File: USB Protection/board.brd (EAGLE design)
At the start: 22.9 x 15.2 mm, 6 parts

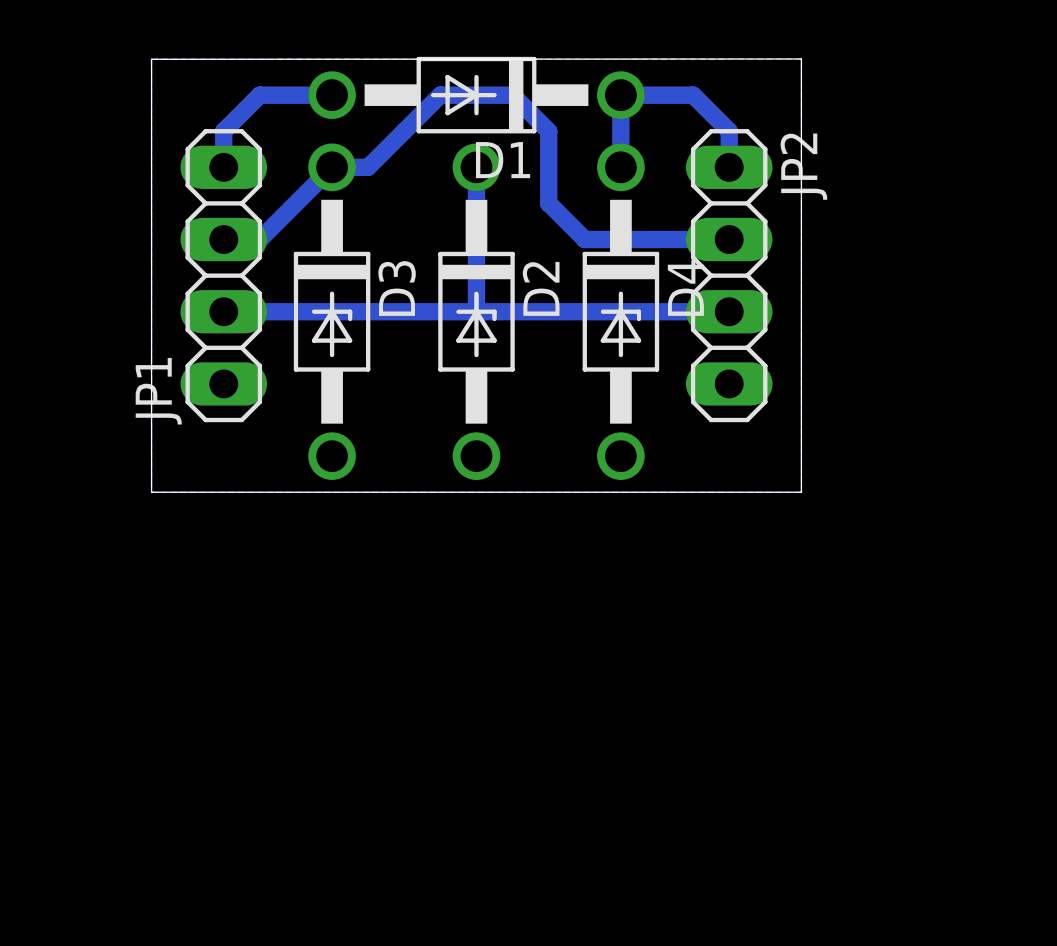
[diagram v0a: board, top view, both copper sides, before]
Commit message: Removed power zener diode
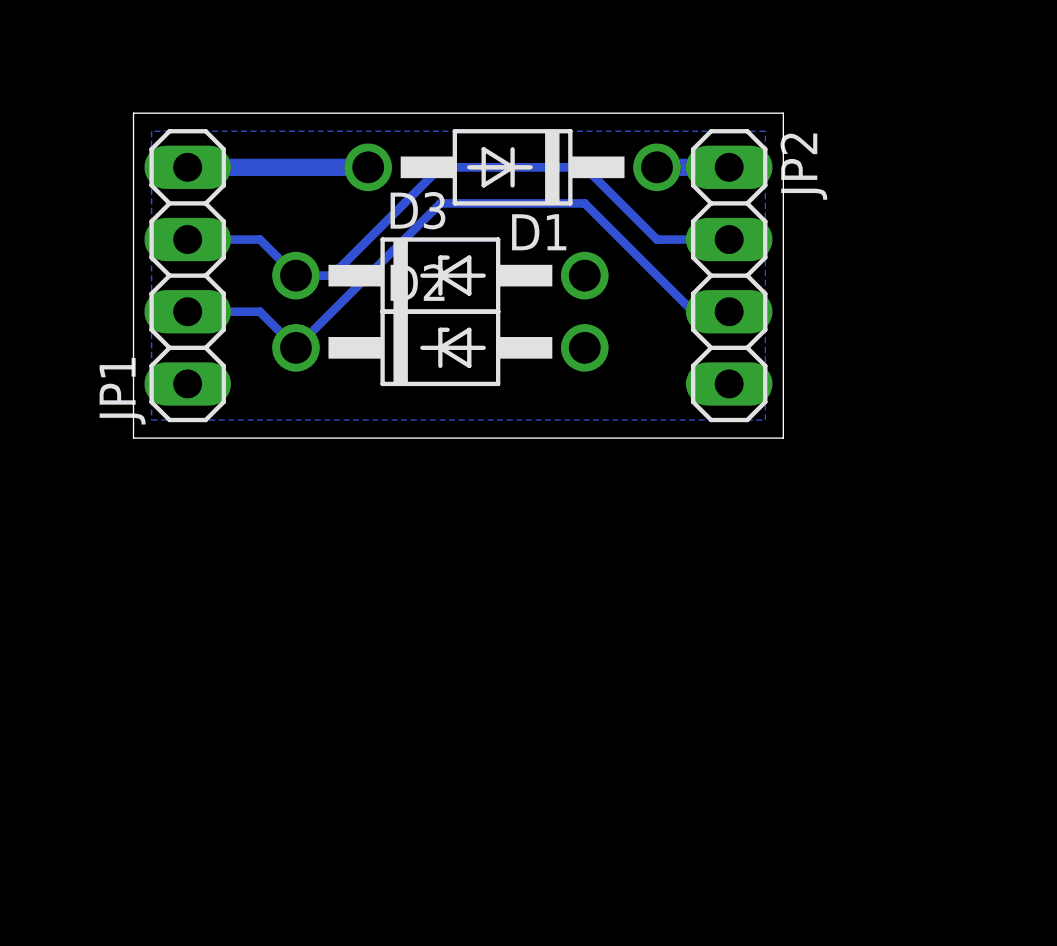
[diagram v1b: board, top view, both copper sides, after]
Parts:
- removed D4: 1N4728, diode:DO41Z10
- moved D3 4.02 mm to (11.4, 25.4), turned to 0 degrees
- moved D1 2.84 mm to (14.0, 29.2)
- moved D2 1.80 mm to (11.4, 22.9), turned to 0 degrees
- moved JP1 1.27 mm to (2.54, 25.4)
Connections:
- net GND: no longer D4.A
- net N$2: no longer D4.C
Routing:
- net N$2: track 8.15 -> 2.54 mm
- net N$6: track 23.5 -> 22.2 mm
- net N$1: track 5.61 -> 6.35 mm
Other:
- board size 22.9 x 15.2 mm -> 22.9 x 11.4 mm
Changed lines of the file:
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@@
 <board>
 <plain>
-<wire x1="1.27" y1="17.78" x2="24.13" y2="17.78" width="0" layer="20"/>
-<wire x1="24.13" y1="17.78" x2="24.13" y2="33.02" width="0" layer="20"/>
-<wire x1="24.13" y1="33.02" x2="1.27" y2="33.01" width="0" layer="20"/>
-<wire x1="1.27" y1="33.01" x2="1.27" y2="17.78" width="0" layer="20"/>
+<wire x1="0.635" y1="19.685" x2="23.495" y2="19.685" width="0" layer="20"/>
+<wire x1="23.495" y1="19.685" x2="23.495" y2="31.115" width="0" layer="20"/>
+<wire x1="23.495" y1="31.115" x2="0.635" y2="31.115" width="0" layer="20"/>
+<wire x1="0.635" y1="31.115" x2="0.635" y2="19.685" width="0" layer="20"/>
 </plain>
 <attributes>
@@
 </autorouter>
 <elements>
-<element name="D1" library="diode" library_urn="urn:adsk.eagle:library:210" package="DO41-10" package3d_urn="urn:adsk.eagle:package:43336/1" value="1N4004" x="12.7" y="31.75" rot="R180"/>
-<element name="D2" library="diode" library_urn="urn:adsk.eagle:library:210" package="DO41Z10" package3d_urn="urn:adsk.eagle:package:43341/1" value="1N4728" x="12.7" y="24.13" rot="R270"/>
-<element name="D3" library="diode" library_urn="urn:adsk.eagle:library:210" package="DO41Z10" package3d_urn="urn:adsk.eagle:package:43341/1" value="1N4728" x="7.62" y="24.13" rot="R270"/>
-<element name="D4" library="diode" library_urn="urn:adsk.eagle:library:210" package="DO41Z10" package3d_urn="urn:adsk.eagle:package:43341/1" value="1N4728" x="17.78" y="24.13" rot="R270"/>
-<element name="JP1" library="pinhead" library_urn="urn:adsk.eagle:library:325" package="1X04" package3d_urn="urn:adsk.eagle:package:22407/2" value="" x="3.81" y="25.4" rot="R90"/>
+<element name="D1" library="diode" library_urn="urn:adsk.eagle:library:210" package="DO41-10" package3d_urn="urn:adsk.eagle:package:43336/1" value="1N4004" x="13.97" y="29.21" rot="R180"/>
+<element name="D2" library="diode" library_urn="urn:adsk.eagle:library:210" package="DO41Z10" package3d_urn="urn:adsk.eagle:package:43341/1" value="1N4728" x="11.43" y="22.86"/>
+<element name="D3" library="diode" library_urn="urn:adsk.eagle:library:210" package="DO41Z10" package3d_urn="urn:adsk.eagle:package:43341/1" value="1N4728" x="11.43" y="25.4"/>
+<element name="JP1" library="pinhead" library_urn="urn:adsk.eagle:library:325" package="1X04" package3d_urn="urn:adsk.eagle:package:22407/2" value="" x="2.54" y="25.4" rot="R90"/>
 <element name="JP2" library="pinhead" library_urn="urn:adsk.eagle:library:325" package="1X04" package3d_urn="urn:adsk.eagle:package:22407/2" value="" x="21.59" y="25.4" rot="R270"/>
 </elements>
@@
 <contactref element="JP1" pad="4"/>
 <contactref element="D1" pad="A"/>
-<wire x1="3.81" y1="29.21" x2="3.81" y2="30.48" width="0.6096" layer="16"/>
-<wire x1="3.81" y1="30.48" x2="5.08" y2="31.75" width="0.6096" layer="16"/>
-<wire x1="5.08" y1="31.75" x2="7.62" y2="31.75" width="0.6096" layer="16"/>
+<wire x1="2.54" y1="29.21" x2="8.89" y2="29.21" width="0.6096" layer="16"/>
 </signal>
 <signal name="N$2">
 <contactref element="D1" pad="C"/>
 <contactref element="JP2" pad="1"/>
-<contactref element="D4" pad="C"/>
-<wire x1="17.78" y1="29.21" x2="17.78" y2="31.75" width="0.6096" layer="16"/>
-<wire x1="17.78" y1="31.75" x2="20.32" y2="31.75" width="0.6096" layer="16"/>
-<wire x1="20.32" y1="31.75" x2="21.59" y2="30.48" width="0.6096" layer="16"/>
-<wire x1="21.59" y1="30.48" x2="21.59" y2="29.21" width="0.6096" layer="16"/>
+<wire x1="19.05" y1="29.21" x2="21.59" y2="29.21" width="0.6096" layer="16"/>
 </signal>
 <signal name="GND">
 <contactref element="JP2" pad="4"/>
-<contactref element="D4" pad="A"/>
 <contactref element="JP1" pad="1"/>
 <contactref element="D2" pad="A"/>
 <contactref element="D3" pad="A"/>
 <polygon width="0.3048" layer="16" isolate="0.6096">
-<vertex x="1.27" y="33.02"/>
-<vertex x="1.27" y="17.78"/>
-<vertex x="24.13" y="17.78"/>
-<vertex x="24.13" y="33.02"/>
+<vertex x="1.27" y="30.48"/>
+<vertex x="1.27" y="20.32"/>
+<vertex x="22.86" y="20.32"/>
+<vertex x="22.86" y="30.48"/>
 </polygon>
 </signal>
@@
 <contactref element="JP2" pad="2"/>
 <contactref element="D3" pad="C"/>
-<wire x1="3.81" y1="26.67" x2="5.08" y2="26.67" width="0.6096" layer="16"/>
-<wire x1="5.08" y1="26.67" x2="7.62" y2="29.21" width="0.6096" layer="16"/>
-<wire x1="7.62" y1="29.21" x2="8.89" y2="29.21" width="0.6096" layer="16"/>
-<wire x1="8.89" y1="29.21" x2="10.16" y2="30.48" width="0.6096" layer="16"/>
-<wire x1="10.16" y1="30.48" x2="11.43" y2="31.75" width="0.6096" layer="16"/>
-<wire x1="11.43" y1="31.75" x2="13.97" y2="31.75" width="0.6096" layer="16"/>
-<wire x1="13.97" y1="31.75" x2="15.24" y2="30.48" width="0.6096" layer="16"/>
-<wire x1="15.24" y1="30.48" x2="15.24" y2="27.94" width="0.6096" layer="16"/>
-<wire x1="15.24" y1="27.94" x2="16.51" y2="26.67" width="0.6096" layer="16"/>
-<wire x1="16.51" y1="26.67" x2="21.59" y2="26.67" width="0.6096" layer="16"/>
+<wire x1="2.54" y1="26.67" x2="5.08" y2="26.67" width="0.3048" layer="16"/>
+<wire x1="6.35" y1="25.4" x2="5.08" y2="26.67" width="0.3048" layer="16"/>
+<wire x1="21.59" y1="26.67" x2="19.05" y2="26.67" width="0.3048" layer="16"/>
+<wire x1="19.05" y1="26.67" x2="16.51" y2="29.21" width="0.3048" layer="16"/>
+<wire x1="16.51" y1="29.21" x2="11.43" y2="29.21" width="0.3048" layer="16"/>
+<wire x1="11.43" y1="29.21" x2="7.62" y2="25.4" width="0.3048" layer="16"/>
+<wire x1="7.62" y1="25.4" x2="6.35" y2="25.4" width="0.3048" layer="16"/>
 </signal>
 <signal name="N$3">
@@
 <contactref element="JP2" pad="3"/>
 <contactref element="D2" pad="C"/>
-<wire x1="12.59863125" y1="24.13" x2="3.81" y2="24.13" width="0.6096" layer="16"/>
-<wire x1="12.59863125" y1="24.13" x2="21.59" y2="24.13" width="0.6096" layer="16"/>
-<wire x1="12.7" y1="29.21" x2="12.7" y2="24.23136875" width="0.6096" layer="16"/>
-<wire x1="12.7" y1="24.23136875" x2="12.59863125" y2="24.13" width="0.6096" layer="16"/>
+<wire x1="2.54" y1="24.13" x2="5.08" y2="24.13" width="0.3048" layer="16"/>
+<wire x1="5.08" y1="24.13" x2="6.35" y2="22.86" width="0.3048" layer="16"/>
+<wire x1="6.35" y1="22.86" x2="11.43" y2="27.94" width="0.3048" layer="16"/>
+<wire x1="11.43" y1="27.94" x2="16.51" y2="27.94" width="0.3048" layer="16"/>
+<wire x1="20.32" y1="24.13" x2="21.59" y2="24.13" width="0.3048" layer="16"/>
+<wire x1="16.51" y1="27.94" x2="20.32" y2="24.13" width="0.3048" layer="16"/>
 </signal>
 </signals>

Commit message: Changed to USB port based connection
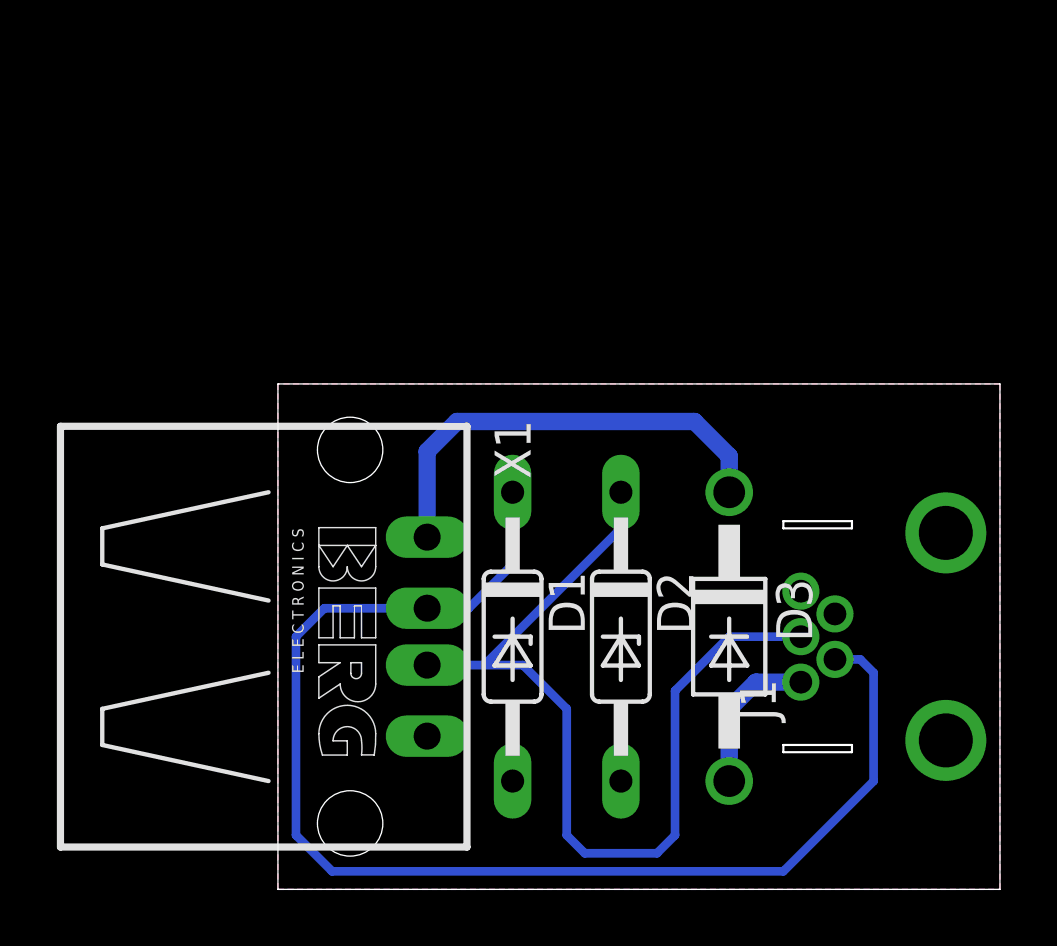
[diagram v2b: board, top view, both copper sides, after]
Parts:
- removed JP1, JP2: (no value), pinhead:1X04
- added J1: USB-MB-H, SparkFun-Retired:USB-MB-H
- added X1: (no value), con-berg:PN87520
- D1: value 1N4004 -> 1N821; device diode:DO41-10 -> diode:DO35Z10
- D2: value 1N4728 -> 1N821; device diode:DO41Z10 -> diode:DO35Z10
- D3: value 1N4728 -> 1N4942; device diode:DO41Z10 -> diode:DO41-10
- moved D1 16.5 mm to (14.0, 12.7), turned to 270 degrees
- moved D3 16.3 mm to (21.6, 12.7), turned to 270 degrees
- moved D2 12.0 mm to (17.8, 12.7), turned to 270 degrees
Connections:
- removed net N$2: D1.C, JP2.1
- removed net N$3: D2.C, JP1.2, JP2.3
- removed net N$6: D3.C, JP1.3, JP2.2
- new net D+: D2.C, J1.D+, X1.3
- new net D-: D1.C, J1.D-, X1.2
- new net VBUS: D3.A, J1.VBUS
- net GND: now also D1.A, J1.GND, X1.4; no longer D3.A, JP1.1, JP2.4
- net N$1: now also D3.C, X1.1; no longer D1.A, JP1.4
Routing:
- net D-: track 0.00 -> 45.7 mm
- net D+: track 0.00 -> 32.7 mm
- net N$3: track 23.3 -> 0.00 mm
- net N$6: track 22.2 -> 0.00 mm
- net N$1: track 6.35 -> 15.9 mm
- net VBUS: track 0.00 -> 5.45 mm
- net N$2: track 2.54 -> 0.00 mm
- added copper zone on layer 1, net GND
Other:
- board size 22.9 x 11.4 mm -> 25.4 x 17.8 mm

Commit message: Started on base board; made board layout for peripherals
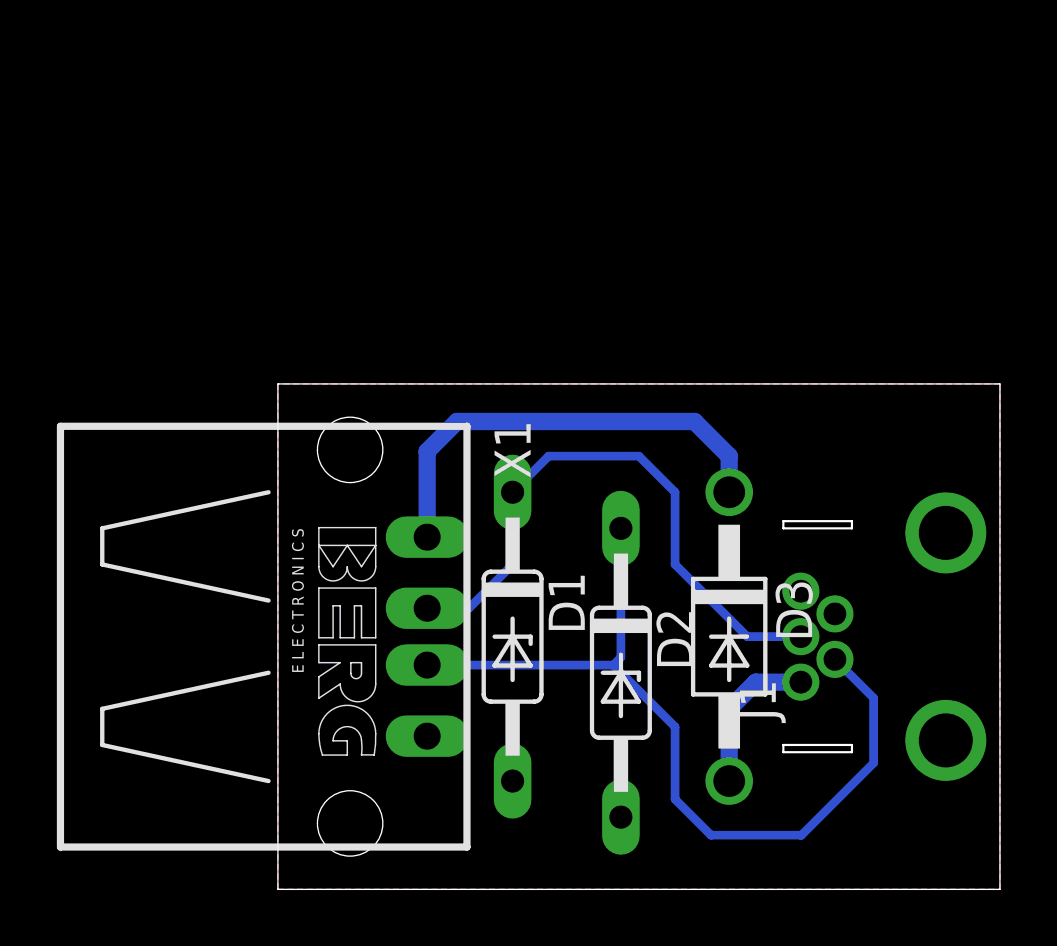
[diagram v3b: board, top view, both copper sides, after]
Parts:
- moved D2 1.27 mm to (17.8, 11.4)
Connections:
- net D+: now also J1.D-; no longer J1.D+
- net D-: now also J1.D+; no longer J1.D-
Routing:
- net D-: track 45.7 -> 21.0 mm
- net D+: track 32.7 -> 29.9 mm
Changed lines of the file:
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@@
 </element>
 <element name="D1" library="diode" library_urn="urn:adsk.eagle:library:210" package="DO35Z10" package3d_urn="urn:adsk.eagle:package:43342/1" value="1N821" x="13.97" y="12.7" rot="R270"/>
-<element name="D2" library="diode" library_urn="urn:adsk.eagle:library:210" package="DO35Z10" package3d_urn="urn:adsk.eagle:package:43342/1" value="1N821" x="17.78" y="12.7" rot="R270"/>
+<element name="D2" library="diode" library_urn="urn:adsk.eagle:library:210" package="DO35Z10" package3d_urn="urn:adsk.eagle:package:43342/1" value="1N821" x="17.78" y="11.43" rot="R270"/>
 <element name="D3" library="diode" library_urn="urn:adsk.eagle:library:210" package="DO41-10" package3d_urn="urn:adsk.eagle:package:43336/1" value="1N4942" x="21.59" y="12.7" rot="R270"/>
 </elements>
@@
 <signal name="D-">
 <contactref element="X1" pad="2"/>
-<contactref element="J1" pad="D-"/>
 <contactref element="D1" pad="C"/>
 <wire x1="12.43" y1="13.7" x2="13.97" y2="15.24" width="0.3048" layer="16"/>
 <wire x1="13.97" y1="15.24" x2="13.97" y2="17.78" width="0.3048" layer="16"/>
-<wire x1="25.31" y1="11.9" x2="26.2" y2="11.9" width="0.3048" layer="16"/>
-<wire x1="26.2" y1="11.9" x2="26.67" y2="11.43" width="0.3048" layer="16"/>
-<wire x1="26.67" y1="11.43" x2="26.67" y2="7.62" width="0.3048" layer="16"/>
-<wire x1="26.67" y1="7.62" x2="23.495" y2="4.445" width="0.3048" layer="16"/>
-<wire x1="7.62" y1="4.445" x2="6.35" y2="5.715" width="0.3048" layer="16"/>
-<wire x1="23.495" y1="4.445" x2="7.62" y2="4.445" width="0.3048" layer="16"/>
 <wire x1="10.965" y1="13.7" x2="12.43" y2="13.7" width="0.3048" layer="16"/>
-<wire x1="6.35" y1="12.7" x2="7.35" y2="13.7" width="0.3048" layer="16"/>
-<wire x1="7.35" y1="13.7" x2="10.965" y2="13.7" width="0.3048" layer="16"/>
-<wire x1="6.35" y1="5.715" x2="6.35" y2="12.7" width="0.3048" layer="16"/>
+<contactref element="J1" pad="D+"/>
+<wire x1="13.97" y1="17.78" x2="15.24" y2="19.05" width="0.3048" layer="16"/>
+<wire x1="15.24" y1="19.05" x2="18.415" y2="19.05" width="0.3048" layer="16"/>
+<wire x1="18.415" y1="19.05" x2="19.685" y2="17.78" width="0.3048" layer="16"/>
+<wire x1="19.685" y1="17.78" x2="19.685" y2="15.24" width="0.3048" layer="16"/>
+<wire x1="19.685" y1="15.24" x2="22.225" y2="12.7" width="0.3048" layer="16"/>
+<wire x1="22.225" y1="12.7" x2="24.11" y2="12.7" width="0.3048" layer="16"/>
 </signal>
 <signal name="D+">
 <contactref element="X1" pad="3"/>
-<contactref element="J1" pad="D+"/>
 <contactref element="D2" pad="C"/>
-<wire x1="12.97" y1="11.7" x2="10.965" y2="11.7" width="0.3048" layer="16"/>
-<wire x1="12.97" y1="11.7" x2="17.78" y2="16.51" width="0.3048" layer="16"/>
-<wire x1="17.78" y1="16.51" x2="17.78" y2="17.78" width="0.3048" layer="16"/>
-<wire x1="19.685" y1="5.715" x2="19.05" y2="5.08" width="0.3048" layer="16"/>
-<wire x1="19.05" y1="5.08" x2="16.51" y2="5.08" width="0.3048" layer="16"/>
-<wire x1="16.51" y1="5.08" x2="15.875" y2="5.715" width="0.3048" layer="16"/>
-<wire x1="15.875" y1="5.715" x2="15.875" y2="10.16" width="0.3048" layer="16"/>
-<wire x1="14.335" y1="11.7" x2="12.97" y2="11.7" width="0.3048" layer="16"/>
-<wire x1="15.875" y1="10.16" x2="14.335" y2="11.7" width="0.3048" layer="16"/>
-<wire x1="24.11" y1="12.7" x2="21.59" y2="12.7" width="0.3048" layer="16"/>
-<wire x1="21.59" y1="12.7" x2="19.685" y2="10.795" width="0.3048" layer="16"/>
-<wire x1="19.685" y1="10.795" x2="19.685" y2="5.715" width="0.3048" layer="16"/>
+<contactref element="J1" pad="D-"/>
+<wire x1="17.51" y1="11.7" x2="10.965" y2="11.7" width="0.3048" layer="16"/>
+<wire x1="17.51" y1="11.7" x2="19.685" y2="9.525" width="0.3048" layer="16"/>
+<wire x1="19.685" y1="9.525" x2="19.685" y2="6.985" width="0.3048" layer="16"/>
+<wire x1="19.685" y1="6.985" x2="20.955" y2="5.715" width="0.3048" layer="16"/>
+<wire x1="20.955" y1="5.715" x2="24.13" y2="5.715" width="0.3048" layer="16"/>
+<wire x1="24.13" y1="5.715" x2="26.67" y2="8.255" width="0.3048" layer="16"/>
+<wire x1="26.67" y1="8.255" x2="26.67" y2="10.54" width="0.3048" layer="16"/>
+<wire x1="26.67" y1="10.54" x2="25.31" y2="11.9" width="0.3048" layer="16"/>
+<wire x1="17.78" y1="16.51" x2="17.78" y2="11.97" width="0.3048" layer="16"/>
+<wire x1="17.78" y1="11.97" x2="17.51" y2="11.7" width="0.3048" layer="16"/>
 </signal>
 <signal name="N$1">
